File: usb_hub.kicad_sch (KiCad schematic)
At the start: 69 parts, among them J5 USB-C_WE_632723300011, J6 USB-C_WE_632723300011, U16 AP7366_SOT, U21 USB7252C, U22 W25Q80DV_USON, U23 TPD4E05U06QDQARQ1, U24 TPD4E05U06QDQARQ1, U25 TPD4E05U06QDQARQ1, U26 TPD4E05U06QDQARQ1, U27 TPD4E05U06QDQARQ1, U28 TPD4E05U06QDQARQ1, Y2 Oscillator_25MHz_ESC_2016MV

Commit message: [#82837] Cleanup USB Hub schematic and add vbus connections
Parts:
- removed C103, C104, C107, C108, C114, C115, C116, C117: C_330n_0402, antmicro-footprints:C_0402_1005Metric, symbol antmicroCapacitors0402:C_330n_0402
- removed C105, C106, C109, C110: C_100n_0201, antmicro-footprints:C_0201, symbol antmicroCapacitorsmisc:C_100n_0201
- removed U23, U26: TPD4E05U06QDQARQ1, antmicro-footprints:USON-10_2.5x1mm_P0.5mm, symbol antmicroTVSDiodes:TPD4E05U06QDQARQ1
- added C103, C81, C82, C83: C_100n_0201, antmicro-footprints:C_0201, symbol antmicroCapacitorsmisc:C_100n_0201
- added C104, C106, C77, C80: C_100n_0402, antmicro-footprints:C_0402_1005Metric, symbol antmicroCapacitors0402:C_100n_0402
- added C105, C78: C_10u_0603, antmicro-footprints:C_0603_1608Metric, symbol antmicroCapacitors0603:C_10u_0603
- added D45, D48: ESD9X5.0ST5G, antmicro-footprints:SOD-923, symbol antmicroTVSDiodes:ESD9X5.0ST5G
- added D47, D49: LED_G_0603_LTST-C190GKT, antmicro-footprints:LED_0603_1608Metric_G, symbol antmicroLEDIndicationDiscrete:LED_G_0603_LTST-C190GKT
- added R257, R258, R69, R70: R_10k_0402, antmicro-footprints:R_0402_1005Metric, symbol antmicroResistors0402:R_10k_0402
- added R259, R73: R_2k2_0402, antmicro-footprints:R_0402_1005Metric, symbol antmicroResistors0402:R_2k2_0402
- added R260, R74: R_470R_0402, antmicro-footprints:R_0402_1005Metric, symbol antmicroResistors0402:R_470R_0402
- added R67, R68: R_1k_0402, antmicro-footprints:R_0402_1005Metric, symbol antmicroResistors0402:R_1k_0402
- added TP43, TP44: TP_0.75mm_SMD, antmicro-footprints:TP_SMD_0.75mm, symbol antmicroTestPoints:TP_0.75mm_SMD
- added U17, U19: TPD4E05U06QDQARQ1, antmicro-footprints:USON-10_2.5x1mm_P0.5mm, symbol antmicroTVSDiodes:TPD4E05U06QDQARQ1
- added U18, U20: AP22615A_TSOT26, antmicro-footprints:TSOT23-6, symbol antmicroPMICPowerDistributionSwitchesLoadDrivers:AP22615A_TSOT26
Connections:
- net +1V12: no longer C100.1, C86.1, C88.1, C90.1, C92.1, C95.1, C97.1, C99.1
- net +3V3: now also R257.2, R67.2, R68.2, R69.2
- net GND: now also C100.1, C86.1, C88.1, C90.1, C92.1, C95.1, C97.1, C99.1, C104.2, C105.2, C106.2, C77.2, C78.2, C80.2, D45.2 (A), D47.1 (C), D48.2 (A), D49.1 (C), R259.1, R73.1, U17.3, U17.8, U18.2 (GND), U19.3, U19.8, U20.2 (GND)
- net USBC3_RX_{1}+: now also J6.B11 (RX_{1}+), U24.1, U24.10
- net USBC3_RX_{1}-: now also J6.B10 (RX_{1}-), U24.2, U24.9
- net USBC3_RX_{2}+: now also J6.A11 (RX_{2}+), U27.1, U27.10
- net USBC3_RX_{2}-: now also J6.A10 (RX_{2}-), U27.2, U27.9
- net USBC4_RX_{1}+: now also J5.B11 (RX_{1}+), U19.1, U19.10
- net USBC4_RX_{1}-: now also J5.B10 (RX_{1}-), U19.2, U19.9
- net USBC4_RX_{2}+: now also J5.A11 (RX_{2}+), U17.1, U17.10
- net USBC4_RX_{2}-: now also J5.A10 (RX_{2}-), U17.2, U17.9
- net USBC4_TX_{1}+: now also C81.2
- net USBC4_TX_{1}-: now also C83.2
- net USBC4_TX_{2}+: now also C82.2
- net USBC4_TX_{2}-: now also C103.2
- net USB3_CC_{1}: now reaches J6.A5 (CC_{1}), U21.12 (DP1_CC1), U28.5, U28.6
- net USB3_CC_{2}: now reaches J6.B5 (CC_{2}), U21.13 (DP1_CC2), U28.4, U28.7
- net USBC3_CONN_TX1_N: now reaches C101.1, J6.A2 (TX_{1}+), U24.4, U24.7
- net USBC3_CONN_TX2_N: now reaches C102.1, J6.B2 (TX_{2}+), U27.4, U27.7
- net USBC4_CONN_TX2_N: now reaches J5.B3 (TX_{2}-)
- net USBC4_CONN_TX2_N: now also C103.1, U17.5, U17.6
- net USBC4_CONN_TX1_N: now reaches J5.A3 (TX_{1}-)
- net USBC4_CONN_TX1_N: now also C83.1, U19.5, U19.6
- net USBC3_CONN_TX1_P: now reaches C112.1, J6.A3 (TX_{1}-), U24.5, U24.6
- net USBC4_CONN_TX1_P: now reaches J5.A2 (TX_{1}+)
- net USBC4_CONN_TX1_P: now also C81.1, U19.4, U19.7
- net USBC4_CONN_TX2_P: now reaches J5.B2 (TX_{2}+)
- net USBC4_CONN_TX2_P: now also C82.1, U17.4, U17.7
- net USBC3_CONN_TX2_P: now reaches C113.1, J6.B3 (TX_{2}-), U27.5, U27.6
- net USBC1_VBUS: now reaches J6.A4 (VBUS), J6.A9 (VBUS), J6.B4 (VBUS), J6.B9 (VBUS)
- net USBC1_VBUS: now also J5.A4 (VBUS), J5.A9 (VBUS), J5.B4 (VBUS), J5.B9 (VBUS), C105.1, C106.1, C78.1, C80.1, D45.1 (C), D48.1 (C), R260.2, R74.2, TP43.1, TP44.1, U18.1 (OUT), U20.1 (OUT)
- net USBHUB_DM renamed USB2.D-
- net USBHUB_DP renamed USB2.D+
- net USBHUB_RXDM renamed USBSS.RX-
- net USBHUB_RXDP renamed USBSS.RX+
- net USBHUB_TXDM renamed USBSS.TX-
- net USBHUB_TXDP renamed USBSS.TX+
- new net: R70.1, U18.4 (EN)
- new net: D47.2 (A), R74.1
- new net: R258.1, U20.4 (EN)
- new net: D49.2 (A), R260.1
- new net +5V: C104.1, C77.1, U18.6 (IN), U20.6 (IN)
- new net USBC1_FLG: R257.1, R69.1, U18.3 (FLG), U20.3 (FLG)
- new net USBC1_ISET: R259.2, R73.2, U18.5 (ISET), U20.5 (ISET)
- new net USBC1_PEN: R258.2, R67.1, R68.1, R70.2
- no-connect marks 34 -> 32
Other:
- moved on the sheet: C100, C101, C102, C111, C112, C113, C76, C79, C84, C85, C86, C87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

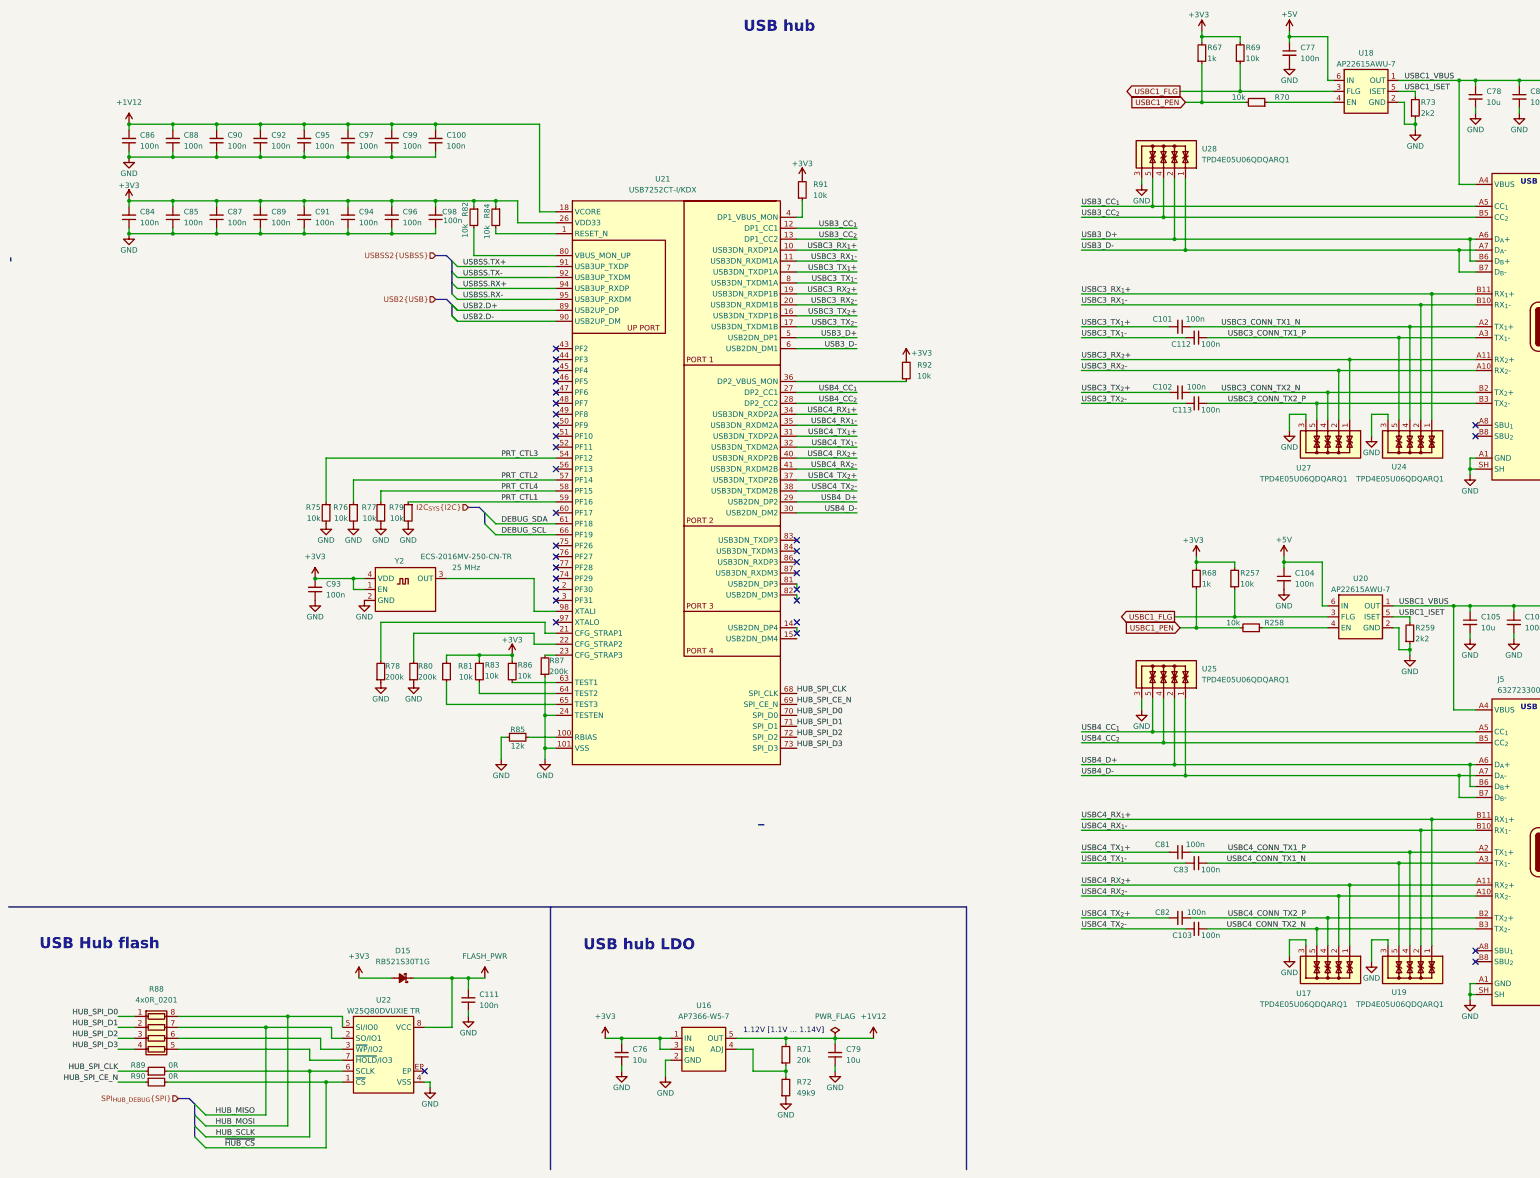
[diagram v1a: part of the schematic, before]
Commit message: [#82837] Fix USB Hub configuration section
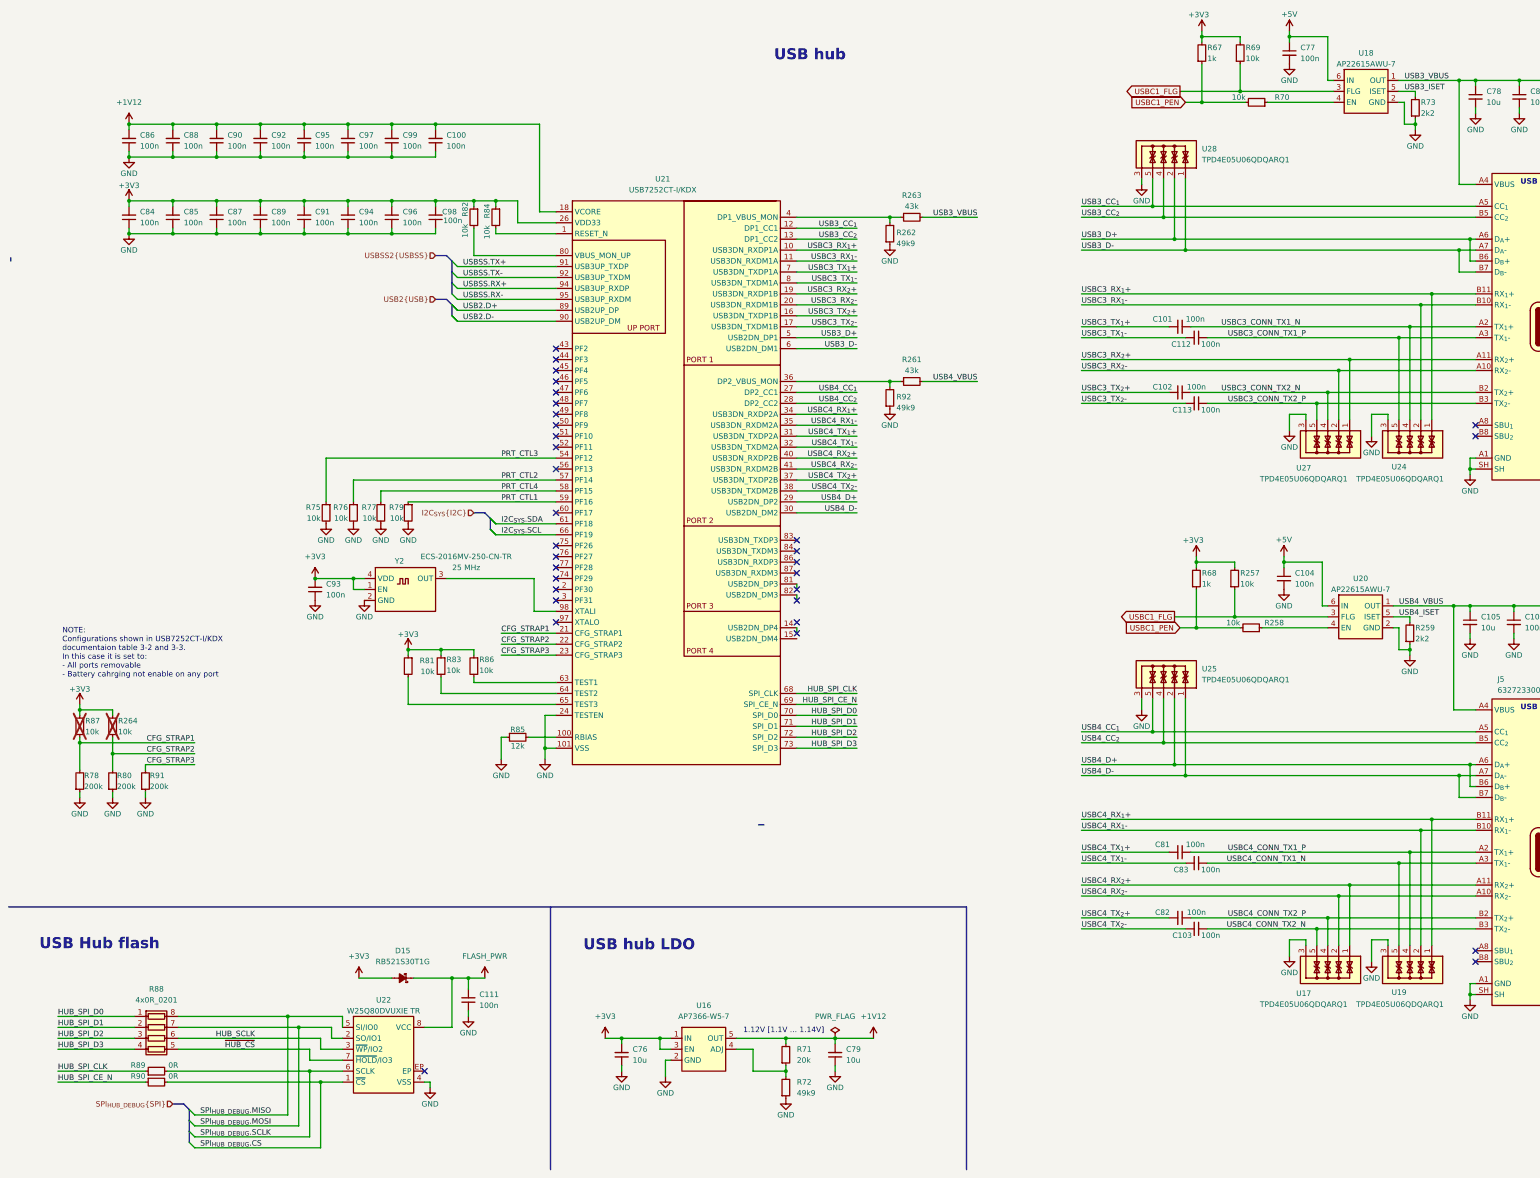
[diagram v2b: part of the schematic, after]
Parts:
- removed R87: R_200k_0402, antmicro-footprints:R_0402_1005Metric, symbol antmicroResistors0402:R_200k_0402
- removed R91, R92: R_10k_0402, antmicro-footprints:R_0402_1005Metric, symbol antmicroResistors0402:R_10k_0402
- added R261, R263: R_43k_0402, antmicro-footprints:R_0402_1005Metric, symbol antmicroResistors0402:R_43k_0402
- added R262, R92: R_49k9_0402, antmicro-footprints:R_0402_1005Metric, symbol antmicroResistors0402:R_49k9_0402
- added R264, R87: R_10k_0402, antmicro-footprints:R_0402_1005Metric, symbol antmicroResistors0402:R_10k_0402
- added R91: R_200k_0402, antmicro-footprints:R_0402_1005Metric, symbol antmicroResistors0402:R_200k_0402
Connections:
- net +3V3: now also R264.2, R87.2
- net GND: now also R262.1, R91.1, R92.1
- net HUB_SCLK: now also R88.6 (R3.2), U22.3 (~{WP}/IO2); no longer R89.2, U22.6 (SCLK)
- net ~{HUB_CS}: now also R88.5 (R4.2), U22.7 (~{HOLD}/IO3); no longer R90.2, U22.1 (~{CS})
- net at U21.4 (DP1_VBUS_MON): now also R262.2, R263.1
- net CFG_STRAP1: now reaches R78.2, U21.21 (CFG_STRAP1)
- net CFG_STRAP1: now also R87.1
- net CFG_STRAP2: now reaches R80.2, U21.22 (CFG_STRAP2)
- net CFG_STRAP2: now also R264.1
- net CFG_STRAP3: now reaches U21.23 (CFG_STRAP3)
- net CFG_STRAP3: now also R91.2
- net at U21.36 (DP2_VBUS_MON): now also R261.1, R92.2
- net DEBUG_SCL renamed I2C_{SYS}.SCL
- net DEBUG_SDA renamed I2C_{SYS}.SDA
- net HUB_MISO renamed SPI_{HUB_DEBUG}.MOSI
- net HUB_MOSI renamed SPI_{HUB_DEBUG}.MISO
- net USBC1_ISET renamed USB3_ISET
- net USB3_ISET: no longer R259.2, U20.5 (ISET)
- net USBC1_VBUS renamed USB3_VBUS
- net USB3_VBUS: now also R263.2; no longer C105.1, C106.1, D48.1 (C), J5.A4 (VBUS), J5.A9 (VBUS), J5.B4 (VBUS), J5.B9 (VBUS), R260.2, TP44.1, U20.1 (OUT)
- new net SPI_{HUB_DEBUG}.CS: R90.2, U22.1 (~{CS})
- new net SPI_{HUB_DEBUG}.SCLK: R89.2, U22.6 (SCLK)
- new net USB4_ISET: R259.2, U20.5 (ISET)
- new net USB4_VBUS: C105.1, C106.1, D48.1 (C), J5.A4 (VBUS), J5.A9 (VBUS), J5.B4 (VBUS), J5.B9 (VBUS), R260.2, R261.2, TP44.1, U20.1 (OUT)
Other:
- note added: "NOTE: Configurations shown in USB7252CT-I/KDX documentaion table 3-2 and 3-3. In this case it is set to: - All ports removable - Battery cahrging not enable on any port"
- moved on the sheet: R78, R80, R81, R83, R86
